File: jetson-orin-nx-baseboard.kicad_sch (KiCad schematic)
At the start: 0 parts

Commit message: Modify project's Title Block
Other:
- company: (none) -> Antmicro Ltd
- title: Jetson Orin Baseboard -> Jetson Orin NX Baseboard
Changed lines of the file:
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@@
   (paper "A4")
   (title_block
-    (title "Jetson Orin Baseboard")
+    (title "Jetson Orin NX Baseboard")
+    (company "Antmicro Ltd")
     (comment 1 "www.antmicro.com")
-    (comment 2 "Antmicro Ltd")
   )
   (image (at 76.99 188.81) (scale 0.15)

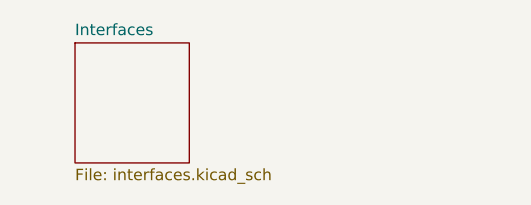
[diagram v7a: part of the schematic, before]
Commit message: Implement FTDI
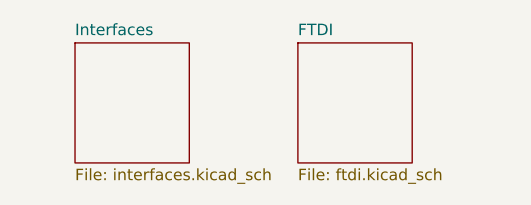
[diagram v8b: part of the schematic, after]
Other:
- added sheet FTDI (ftdi.kicad_sch)
